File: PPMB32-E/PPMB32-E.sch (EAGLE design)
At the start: 1 part, among them U1 ESP32-DEVKITC-32D

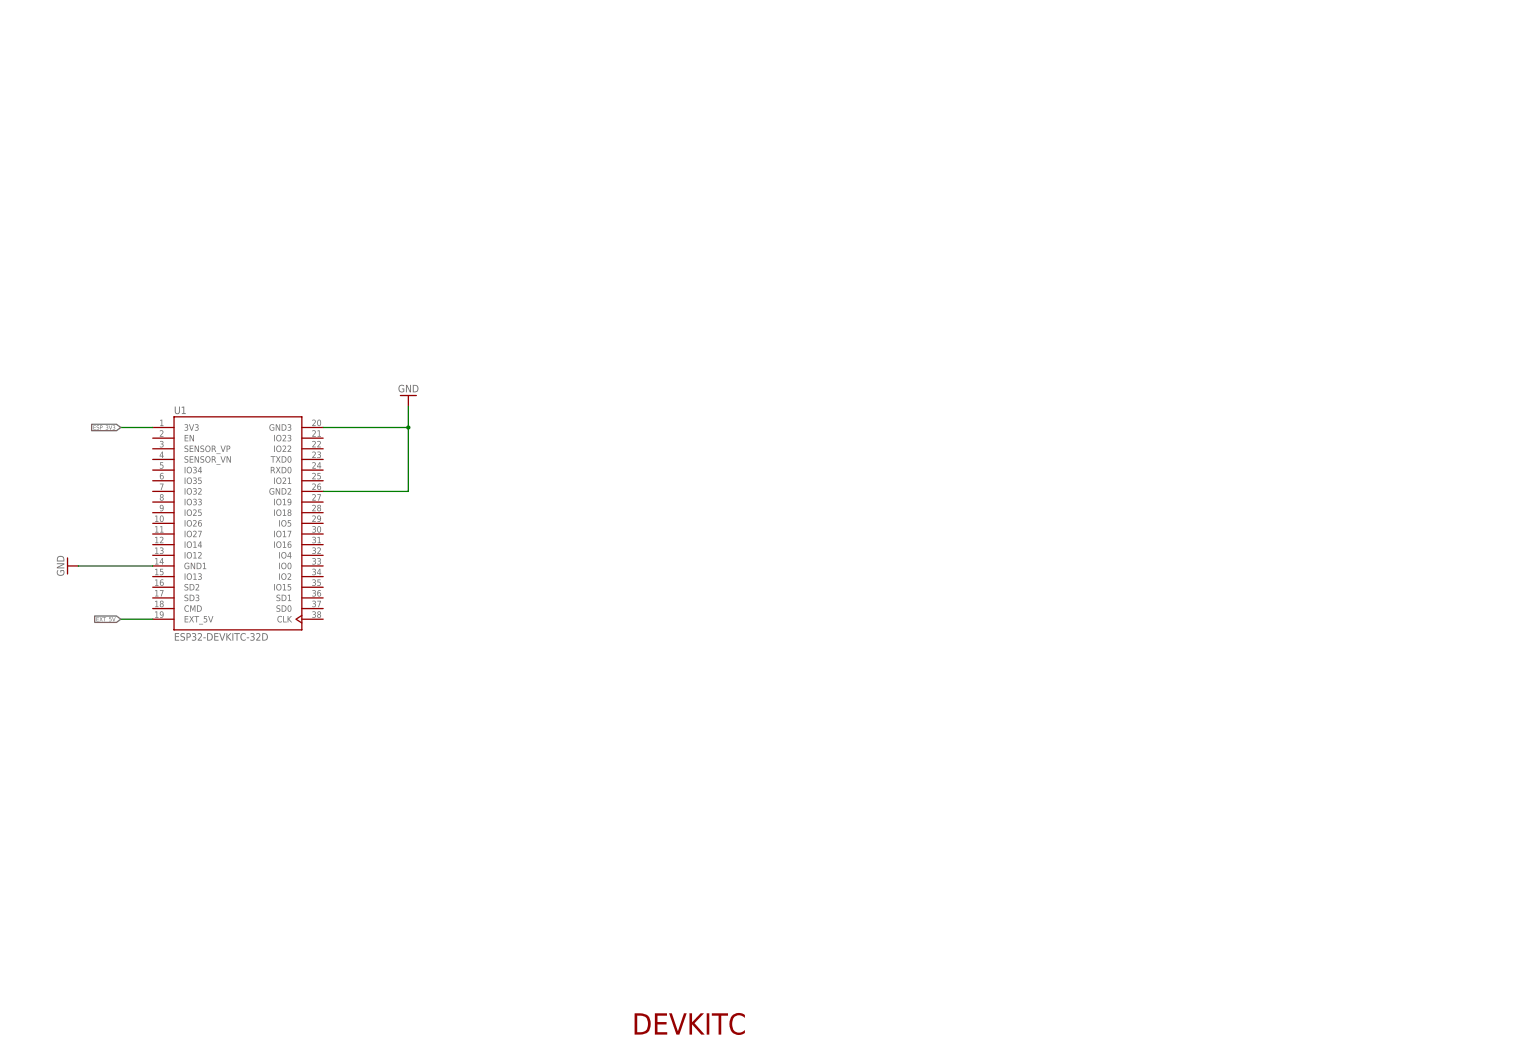
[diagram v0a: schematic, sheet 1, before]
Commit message: Made major advances in PPMB32-E scheme. Started routing PPMB32-E
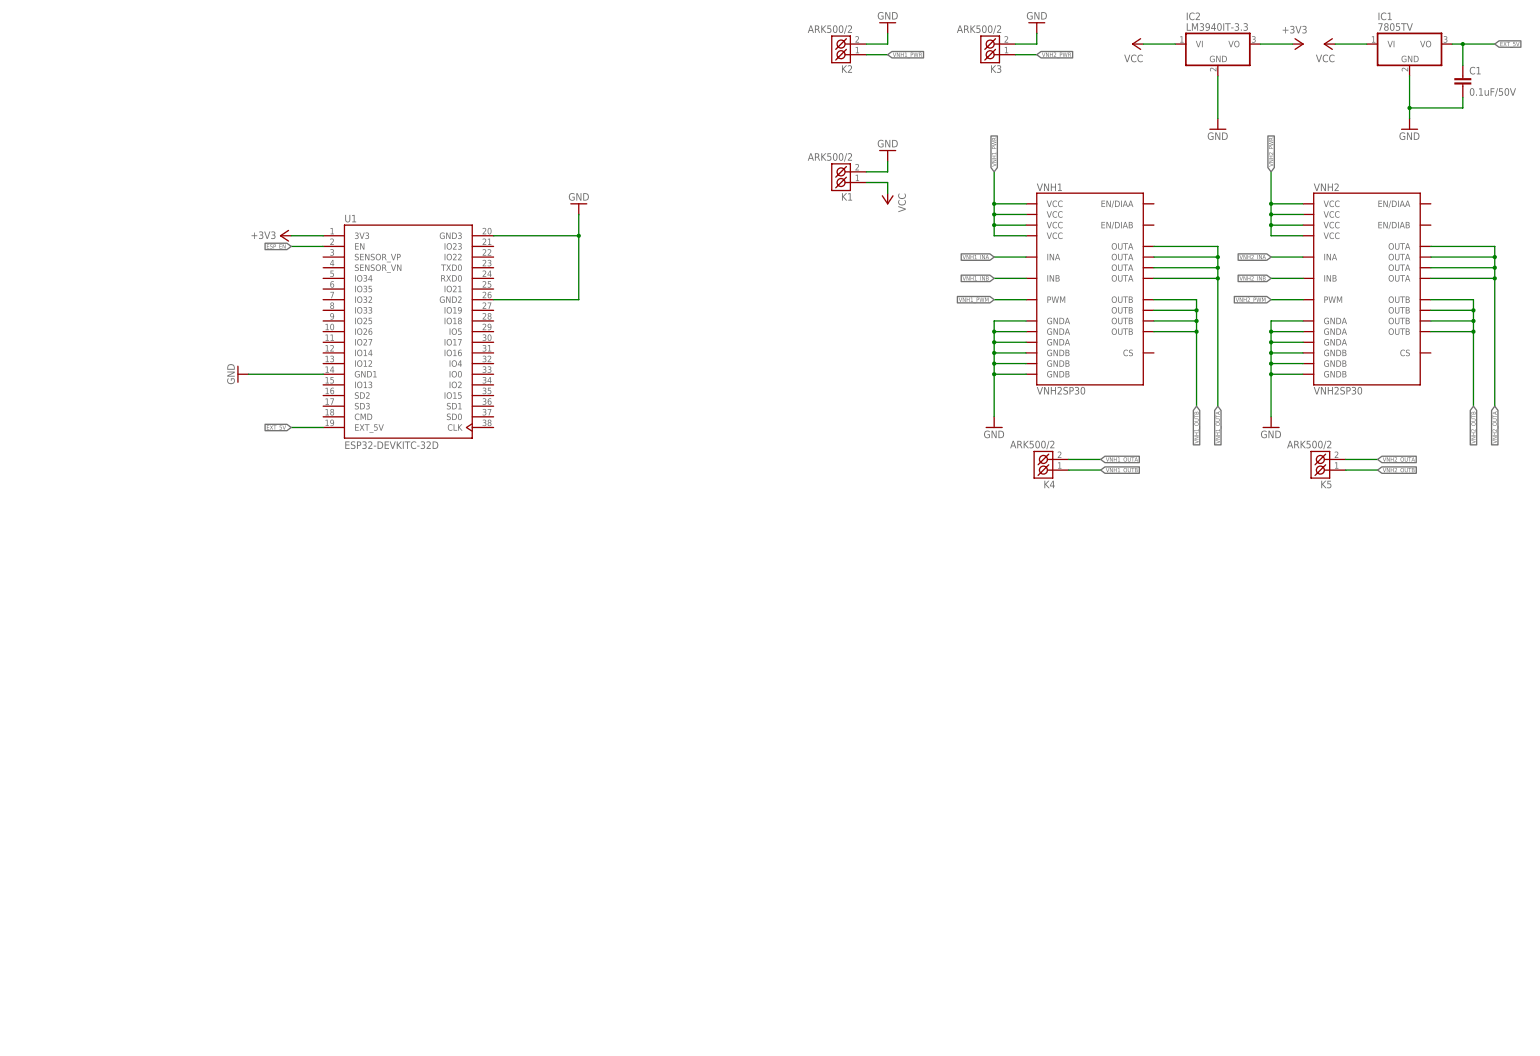
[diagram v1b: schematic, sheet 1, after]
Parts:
- added C1: 0.1uF/50V, rcl:C-EUC1206K
- added IC1: 7805TV, linear:7805TV
- added IC2: LM3940IT-3.3, linear:788TV
- added K1, K2, K3, K4, K5: ARK500/2, #PaJa_konektory:ARK500/2
- added VNH1, VNH2: VNH2SP30, SparkFun-IC-Special-Function:VNH2SP30
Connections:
- removed net ESP_3V3: U1.3V3
- new net +3V3: IC2.VO, U1.3V3
- new net ESP_EN: U1.EN
- new net VCC: IC1.VI, IC2.VI, K1.K1
- new net VNH1_INA: VNH1.INA
- new net VNH1_INB: VNH1.INB
- new net VNH1_OUTA: K4.K2, VNH1.OUTA@1, VNH1.OUTA@25, VNH1.OUTA@30, VNH1.OUTA@SLUG3
- new net VNH1_OUTB: K4.K1, VNH1.OUTB@15, VNH1.OUTB@16, VNH1.OUTB@21, VNH1.OUTB@SLUG2
- new net VNH1_PWM: VNH1.PWM
- new net VNH1_PWR: K2.K1, VNH1.VCC@13, VNH1.VCC@23, VNH1.VCC@3, VNH1.VCC@SLUG1
- new net VNH2_INA: VNH2.INA
- new net VNH2_INB: VNH2.INB
- new net VNH2_OUTA: K5.K2, VNH2.OUTA@1, VNH2.OUTA@25, VNH2.OUTA@30, VNH2.OUTA@SLUG3
- new net VNH2_OUTB: K5.K1, VNH2.OUTB@15, VNH2.OUTB@16, VNH2.OUTB@21, VNH2.OUTB@SLUG2
- new net VNH2_PWM: VNH2.PWM
- new net VNH2_PWR: K3.K1, VNH2.VCC@13, VNH2.VCC@23, VNH2.VCC@3, VNH2.VCC@SLUG1
- net EXT_5V: now also C1.1, IC1.VO
- net GND: now also C1.2, IC1.GND, IC2.GND, K1.K2, K2.K2, K3.K2, VNH1.GNDA@26, VNH1.GNDA@27, VNH1.GNDA@28, VNH1.GNDB@18, VNH1.GNDB@19, VNH1.GNDB@20, VNH2.GNDA@26, VNH2.GNDA@27, VNH2.GNDA@28, VNH2.GNDB@18, VNH2.GNDB@19, VNH2.GNDB@20
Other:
- note removed: "DEVKITC"
- moved on the sheet: U1

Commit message: Made progress on PPMB32-E scheme and board. Minor fixes in PPMB32-F board
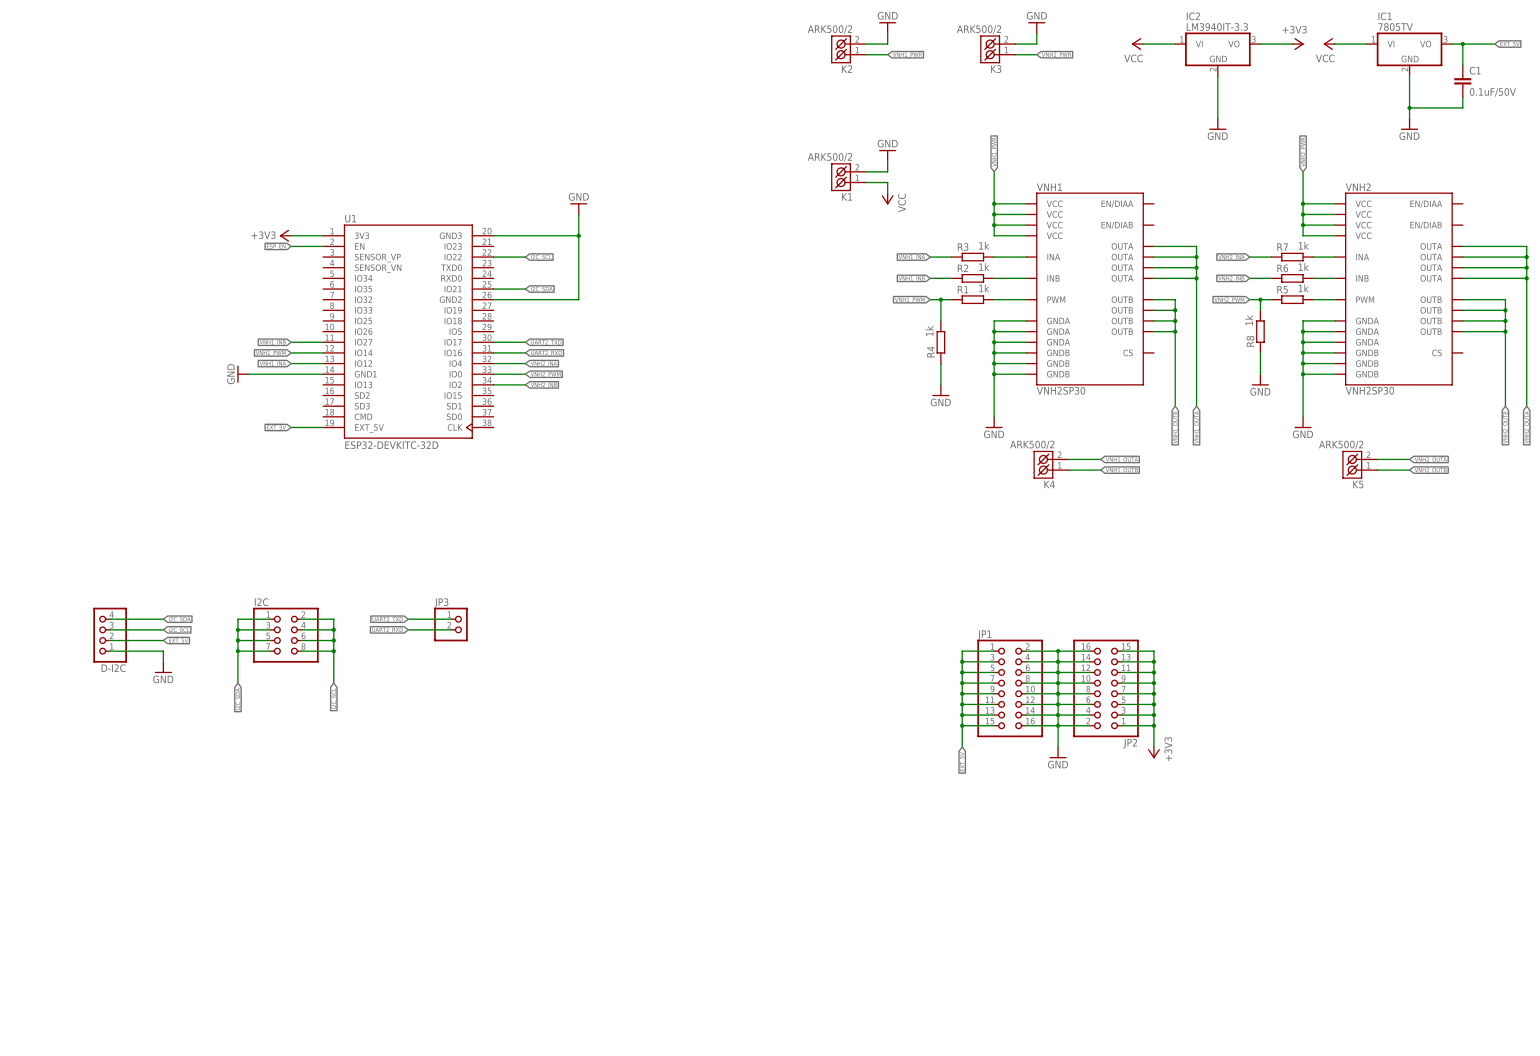
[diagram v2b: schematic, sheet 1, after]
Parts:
- added D-I2C: (no value), pinhead:PINHD-1X4
- added I2C: (no value), pinhead:PINHD-2X4
- added JP1, JP2: (no value), pinhead:PINHD-2X8
- added JP3: (no value), pinhead:PINHD-1X2
- added R1, R2, R3, R4, R5, R6, R7, R8: 1k, rcl:R-EU_R0603
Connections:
- new net I2C_SCL: D-I2C.3, I2C.2, I2C.4, I2C.6, I2C.8, U1.IO22
- new net I2C_SDA: D-I2C.4, I2C.1, I2C.3, I2C.5, I2C.7, U1.IO21
- new net N$1: R3.2, VNH1.INA
- new net N$2: R2.2, VNH1.INB
- new net N$3: R1.2, VNH1.PWM
- new net N$5: R5.2, VNH2.PWM
- new net N$6: R6.2, VNH2.INB
- new net N$7: R7.2, VNH2.INA
- new net UART2_RXD: JP3.2, U1.IO16
- new net UART2_TXD: JP3.1, U1.IO17
- net +3V3: now also JP2.1, JP2.11, JP2.13, JP2.15, JP2.3, JP2.5, JP2.7, JP2.9
- net EXT_5V: now also D-I2C.2, JP1.1, JP1.11, JP1.13, JP1.15, JP1.3, JP1.5, JP1.7, JP1.9
- net GND: now also D-I2C.1, JP1.10, JP1.12, JP1.14, JP1.16, JP1.2, JP1.4, JP1.6, JP1.8, JP2.10, JP2.12, JP2.14, JP2.16, JP2.2, JP2.4, JP2.6, JP2.8, R4.1, R8.1
- net VNH1_INA: now also R3.1, U1.IO12; no longer VNH1.INA
- net VNH1_INB: now also R2.1, U1.IO27; no longer VNH1.INB
- net VNH1_PWM: now also R1.1, R4.2, U1.IO14; no longer VNH1.PWM
- net VNH2_INA: now also R7.1, U1.IO4; no longer VNH2.INA
- net VNH2_INB: now also R6.1, U1.IO2; no longer VNH2.INB
- net VNH2_PWM: now also R5.1, R8.2, U1.IO0; no longer VNH2.PWM
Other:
- moved on the sheet: K5, VNH2

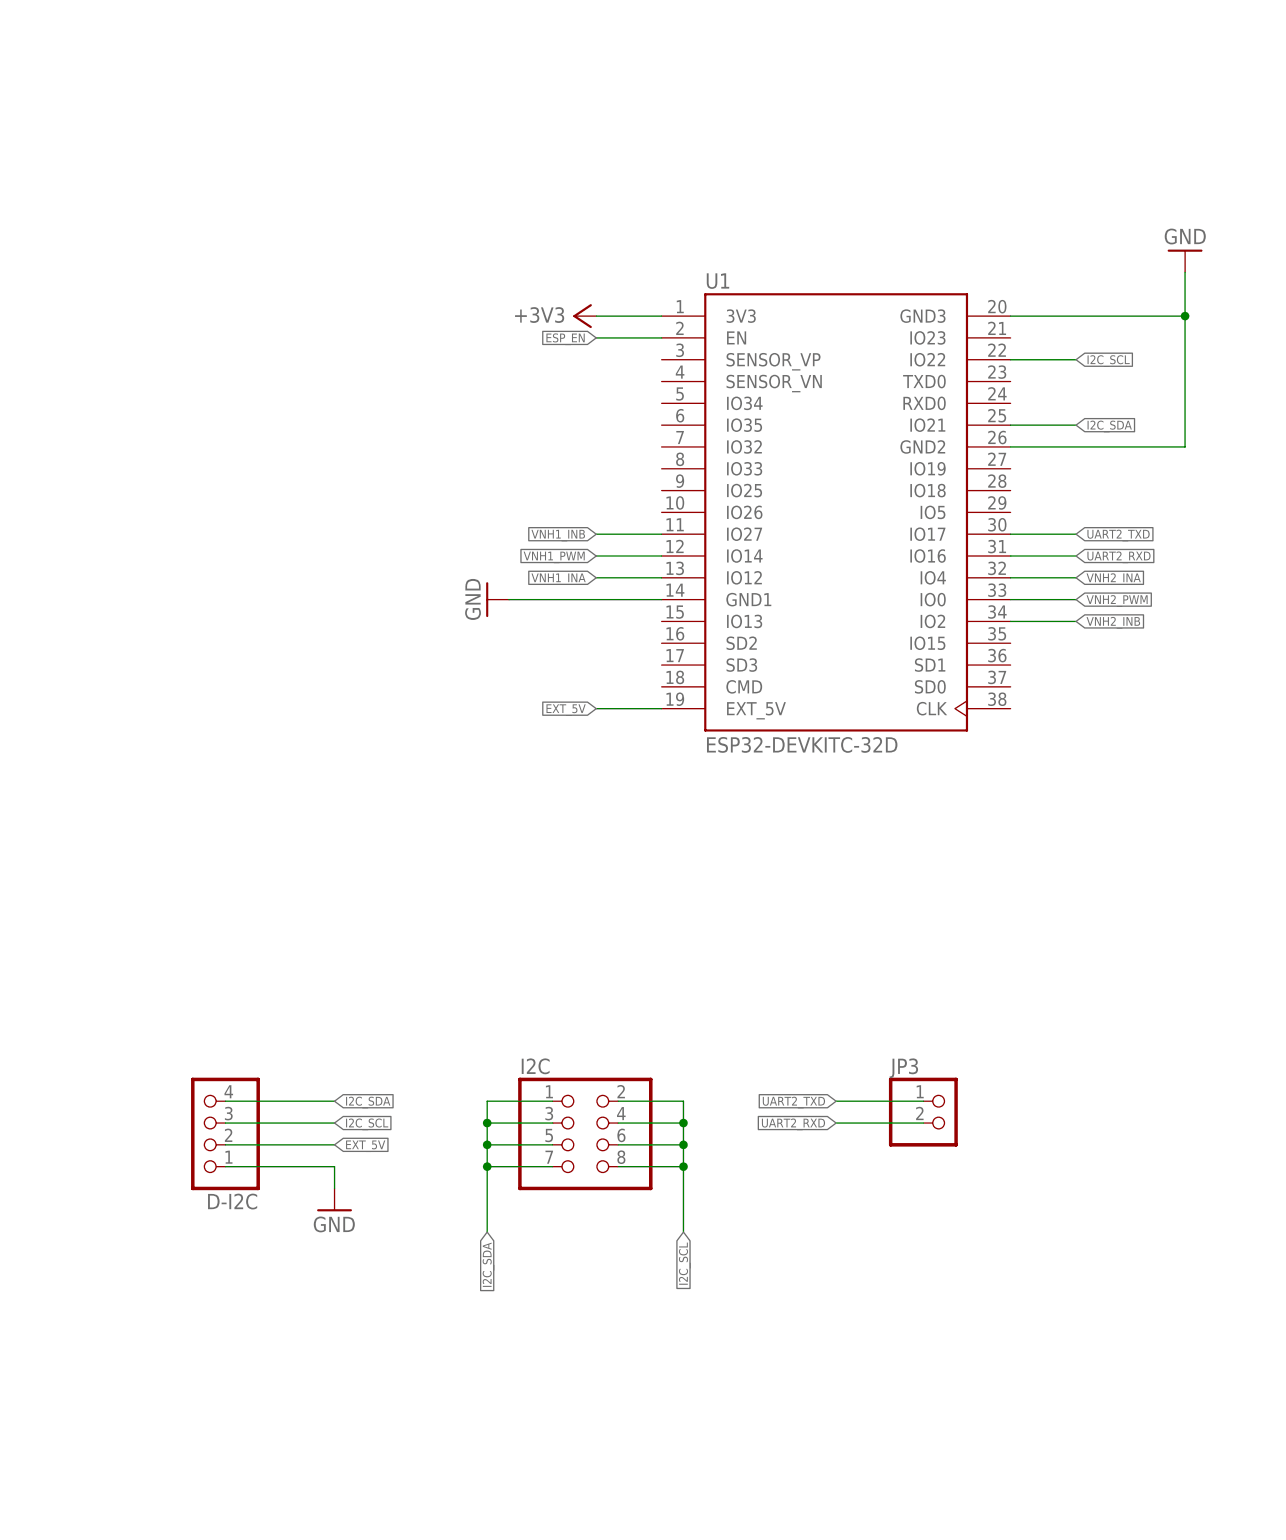
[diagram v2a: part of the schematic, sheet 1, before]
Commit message: Progress on routing PPMB32-E
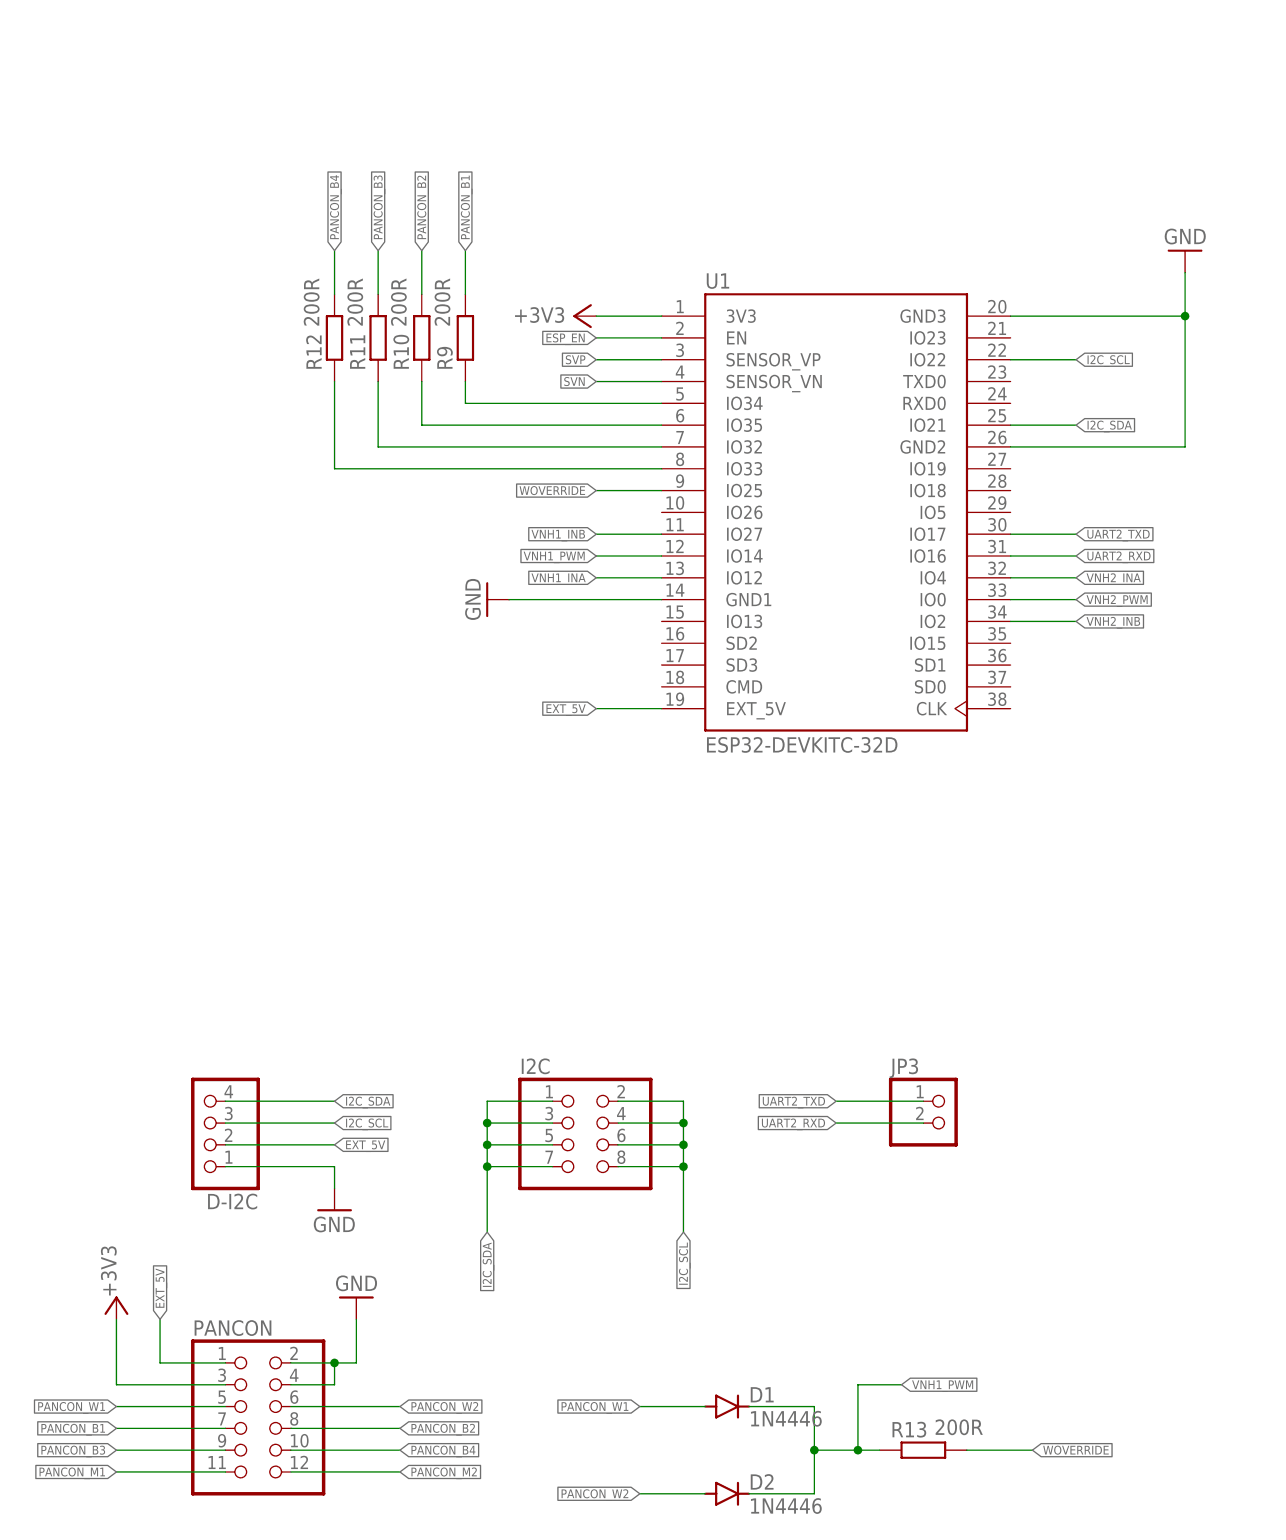
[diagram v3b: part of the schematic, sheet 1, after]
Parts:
- added D1, D2: 1N4446, diode:1N4446
- added PANCON: (no value), pinhead:PINHD-2X6
- added R10, R11, R12, R13, R9: 200R, rcl:R-EU_R0603
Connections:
- new net N$10: R12.1, U1.IO33
- new net N$4: R9.1, U1.IO34
- new net N$8: R10.1, U1.IO35
- new net N$9: R11.1, U1.IO32
- new net PANCON_B1: PANCON.7, R9.2
- new net PANCON_B2: PANCON.8, R10.2
- new net PANCON_B3: PANCON.9, R11.2
- new net PANCON_B4: PANCON.10, R12.2
- new net PANCON_M1: PANCON.11
- new net PANCON_M2: PANCON.12
- new net PANCON_W1: D1.A, PANCON.5
- new net PANCON_W2: D2.A, PANCON.6
- new net SVN: U1.SENSOR_VN
- new net SVP: U1.SENSOR_VP
- new net WOVERRIDE: R13.2, U1.IO25
- net +3V3: now also PANCON.3
- net EXT_5V: now also PANCON.1
- net GND: now also PANCON.2, PANCON.4
- net VNH1_PWM: now also D1.C, D2.C, R13.1

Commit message: Major changes in PPMB32-E board and scheme
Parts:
- added C2: 0.33uF, rcl:C-EUC1206K
- added C3: 33uF, rcl:C-EUC1206K
- added C4: 0.47uF, rcl:C-EUC1206K
- added OBDHT: DHT22, diy-modules:TEMP-HUM-SENSOR-DHT22
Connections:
- new net GPIO23: U1.IO23
- new net GPIO26: U1.IO26
- new net GPIO5: U1.IO5
- new net INTERNAL_SENS: U1.IO13
- new net N$13: OBDHT.DAT
- new net ONE_WIRE: U1.IO15
- new net UART0_RXD: U1.RXD0
- new net UART0_TXD: U1.TXD0
- new net UART2_CTS: U1.IO19
- new net UART2_RTS: U1.IO18
- net +3V3: now also C3.1, OBDHT.VDD
- net EXT_5V: now also C4.1, IC2.VI
- net GND: now also C2.2, C3.2, C4.2, OBDHT.GND
- net UART2_RXD: now also U1.IO17; no longer U1.IO16
- net UART2_TXD: now also U1.IO16; no longer U1.IO17
- net VCC: now also C2.1; no longer IC2.VI
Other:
- moved on the sheet: C1, IC1, IC2, JP1, JP2
